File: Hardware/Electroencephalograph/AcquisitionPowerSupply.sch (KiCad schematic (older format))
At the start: 28 parts, among them U10 TPS60403, U7 LP5912-1.8DRVT, U8 LP5912-1.8DRVT, U9 LP5912-1.8DRVT

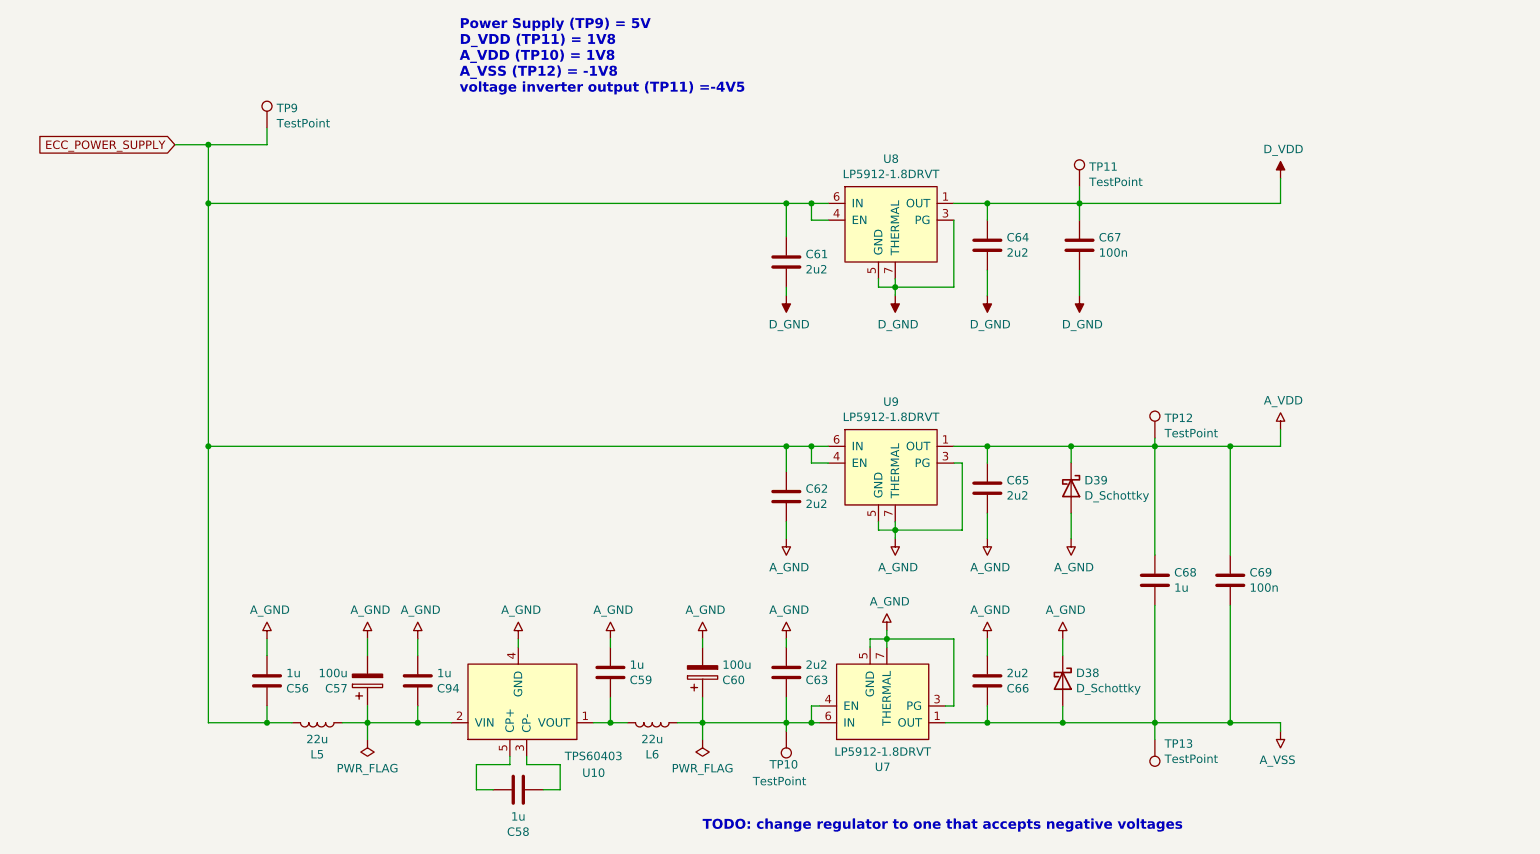
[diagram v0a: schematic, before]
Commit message: choosed other stgabilisators due to obscolence of previous ones
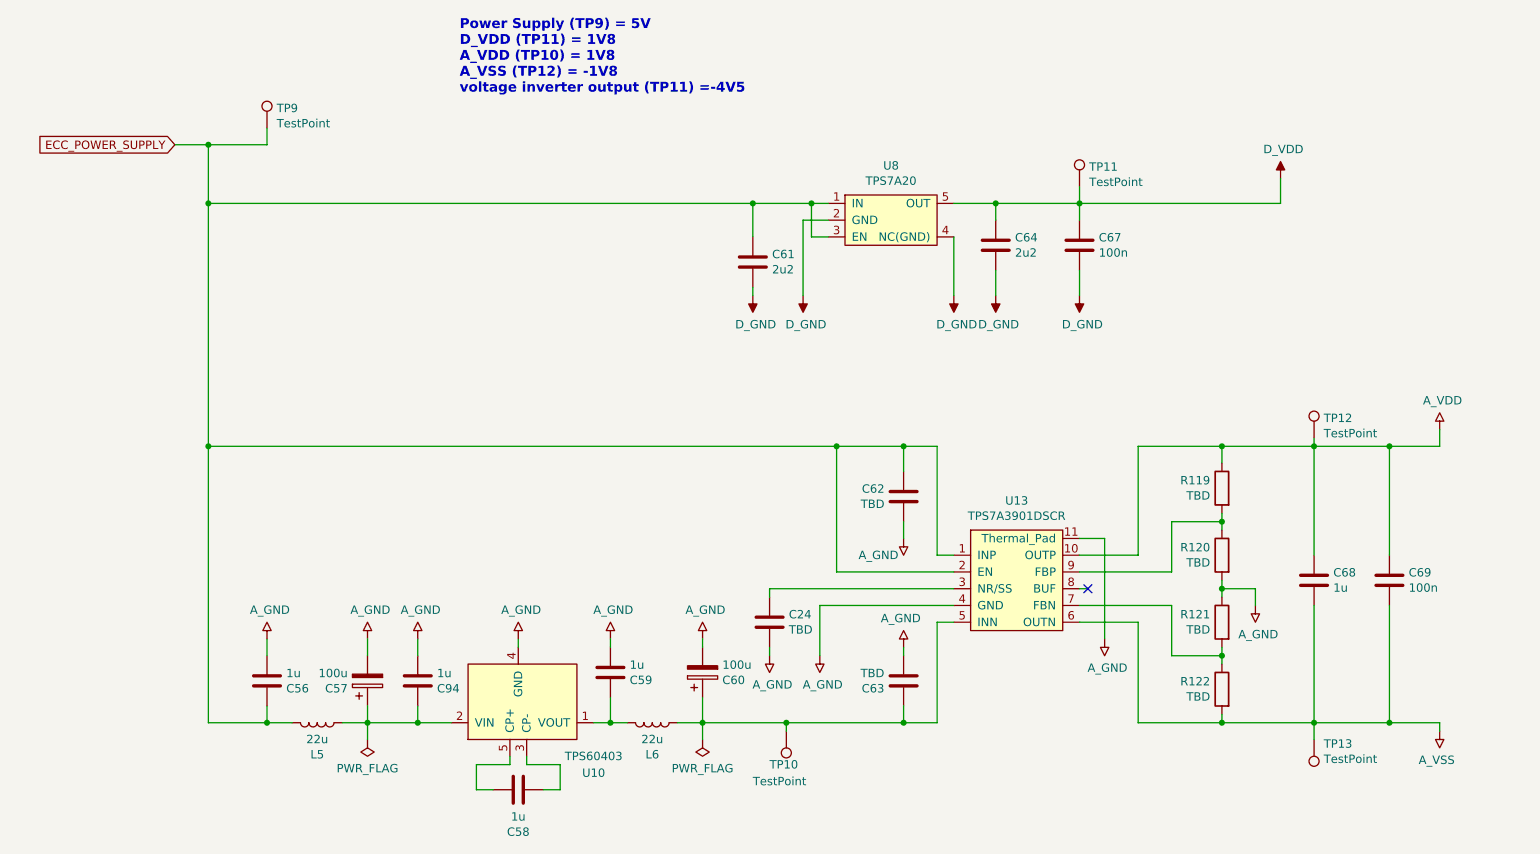
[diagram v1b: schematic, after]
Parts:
- removed C65, C66: 2u2, Capacitor_SMD:C_0402_1005Metric, symbol Device:C
- removed D38, D39: D_Schottky, Diode_SMD:D_0805_2012Metric, symbol Device:D_Schottky
- removed U7, U8, U9: LP5912-1.8DRVT, Package_SON:WSON-8-1EP_2x2mm_P0.5mm_EP0.9x1.6mm_ThermalVias, symbol Electroencephalograph:LP5912-1.8DRVT
- added C24: TBD, Capacitor_SMD:C_0402_1005Metric, symbol Device:C
- added R119, R120, R121, R122: TBD, Resistor_SMD:R_0402_1005Metric, symbol Device:R
- added U13: TPS7A3901DSCR, symbol Electroencephalograph:TPS7A3901DSCR
- added U8: TPS7A20, Package_TO_SOT_SMD:SOT-23-5, symbol Electroencephalograph:TPS7A20
- C62, C63: value 2u2 -> TBD
- TP11, TP9: footprint TestPoint:TestPoint_Pad_1.5x1.5mm -> TestPoint:TestPoint_Pad_D1.0mm
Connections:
- net A_GND: now also C24.2, R120.2, R121.1, U13.11 (Thermal_Pad), U13.4 (GND)
- net A_VDD: now also R119.1, U13.10 (OUTP)
- net A_VSS: now also R122.2, U13.6 (OUTN)
- net D_GND: now also U8.2 (GND), U8.4 (NC(GND))
- net D_VDD: now also U8.5 (OUT)
- net ECC_POWER_SUPPLY: now also U13.1 (INP), U13.2 (EN), U8.1 (IN), U8.3 (EN)
- net at C60.1, C63.1, L6.1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: now also U13.5 (INN)
- new net: C24.1, U13.3 (NR/SS)
- new net: R121.2, R122.1, U13.7 (FBN)
- new net: R119.2, R120.1, U13.9 (FBP)
- no-connect marks 0 -> 1
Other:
- note removed: "TODO: change regulator to one that accepts negative voltages"
- moved on the sheet: C61, C62, C64, C68, C69, TP12, TP13

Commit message: Finished design of PCB.
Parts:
- removed R119, R120, R121, R122: TBD, Resistor_SMD:R_0402_1005Metric, symbol Device:R
- removed TP12: TestPoint, TestPoint:TestPoint_Pad_1.5x1.5mm, symbol Connector:TestPoint
- removed U13: TPS7A3901DSCR, symbol Electroencephalograph:TPS7A3901DSCR
- added C65: 10n, Capacitor_SMD:C_0402_1005Metric, symbol Device:C
- added C66, C77: 2u2, Capacitor_SMD:C_0402_1005Metric, symbol Device:C
- added C76: 100n, Capacitor_SMD:C_0402_1005Metric, symbol Device:C
- added JP4: Jumper_NC_Small, Jumper:SolderJumper-2_P1.3mm_Bridged_Pad1.0x1.5mm, symbol Device:Jumper_NC_Small
- added TP20: TestPoint, TestPoint:TestPoint_Pad_D1.0mm, symbol Connector:TestPoint
- added U7: TPS7A20, Package_TO_SOT_SMD:SOT-23-5, symbol Electroencephalograph:TPS7A20
- added U9: TPS72325DBVT, Package_TO_SOT_SMD:SOT-23-5, symbol Electroencephalograph:TPS72325DBVT
- C24, C63: value TBD -> 2u2
- C62: value TBD -> 100n
- TP10, TP13: footprint TestPoint:TestPoint_Pad_1.5x1.5mm -> TestPoint:TestPoint_Pad_D1.0mm
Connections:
- net A_GND: now also C65.2, C66.2, C76.2, C77.2, U7.2 (GND), U7.4 (NC(GND)), U9.1 (GND)
- net A_VDD: now also C24.1, C62.1, TP20.1, U7.5 (OUT)
- net A_VSS: now also C66.1, C76.1, U9.5 (OUT)
- net ECC_POWER_SUPPLY: now also C63.1, U7.1 (IN), U7.3 (EN); no longer C62.1
- net at C60.1, L6.1, TP10.1: now also C77.1, JP4.1, U9.2 (IN); no longer C63.1
- new net: JP4.2, U9.3 (EN)
- new net: C65.1, U9.4 (NR)
- no-connect marks 1 -> 0
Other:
- moved on the sheet: C59, L6, TP10, TP13

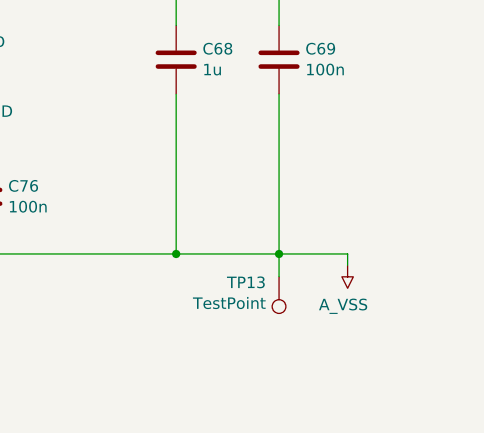
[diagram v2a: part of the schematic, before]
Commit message: add bom
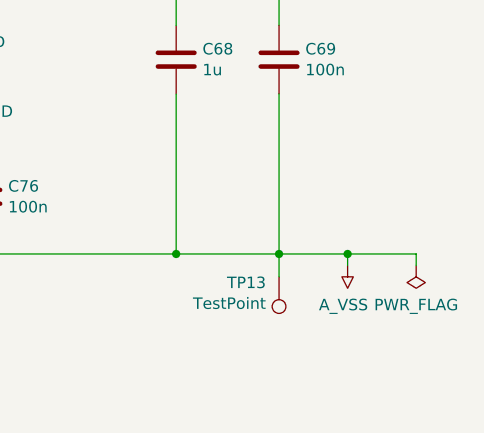
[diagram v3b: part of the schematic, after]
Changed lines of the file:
@@
 	1    0    0    1
 $EndComp
+$Comp
+L power:PWR_FLAG #FLG?
+U 1 1 60DE7611
+P 9500 5550
+F 0 "#FLG?" H 9500 5625 50  0001 C CNN
+F 1 "PWR_FLAG" H 9500 5723 50  0000 C CNN
+F 2 "" H 9500 5550 50  0001 C CNN
+F 3 "~" H 9500 5550 50  0001 C CNN
+	1    9500 5550
+	-1   0    0    1
+$EndComp
+Wire Wire Line
+	9200 5500 9500 5500
+Connection ~ 9200 5500
+Wire Wire Line
+	9500 5500 9500 5550
 $EndSCHEMATC
